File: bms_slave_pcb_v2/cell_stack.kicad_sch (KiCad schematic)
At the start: 33 parts, among them J10 Module Bottom Left FPC Female, J11 Module Bottom Right FPC Female, J4 Module Top Left FPC Female, J5 Module Top Right FPC Female, J6 Breadboard pins for testing, J7 Breadboard pins for testing, J8 Breadboard pins for testing, J9 Breadboard pins for testing

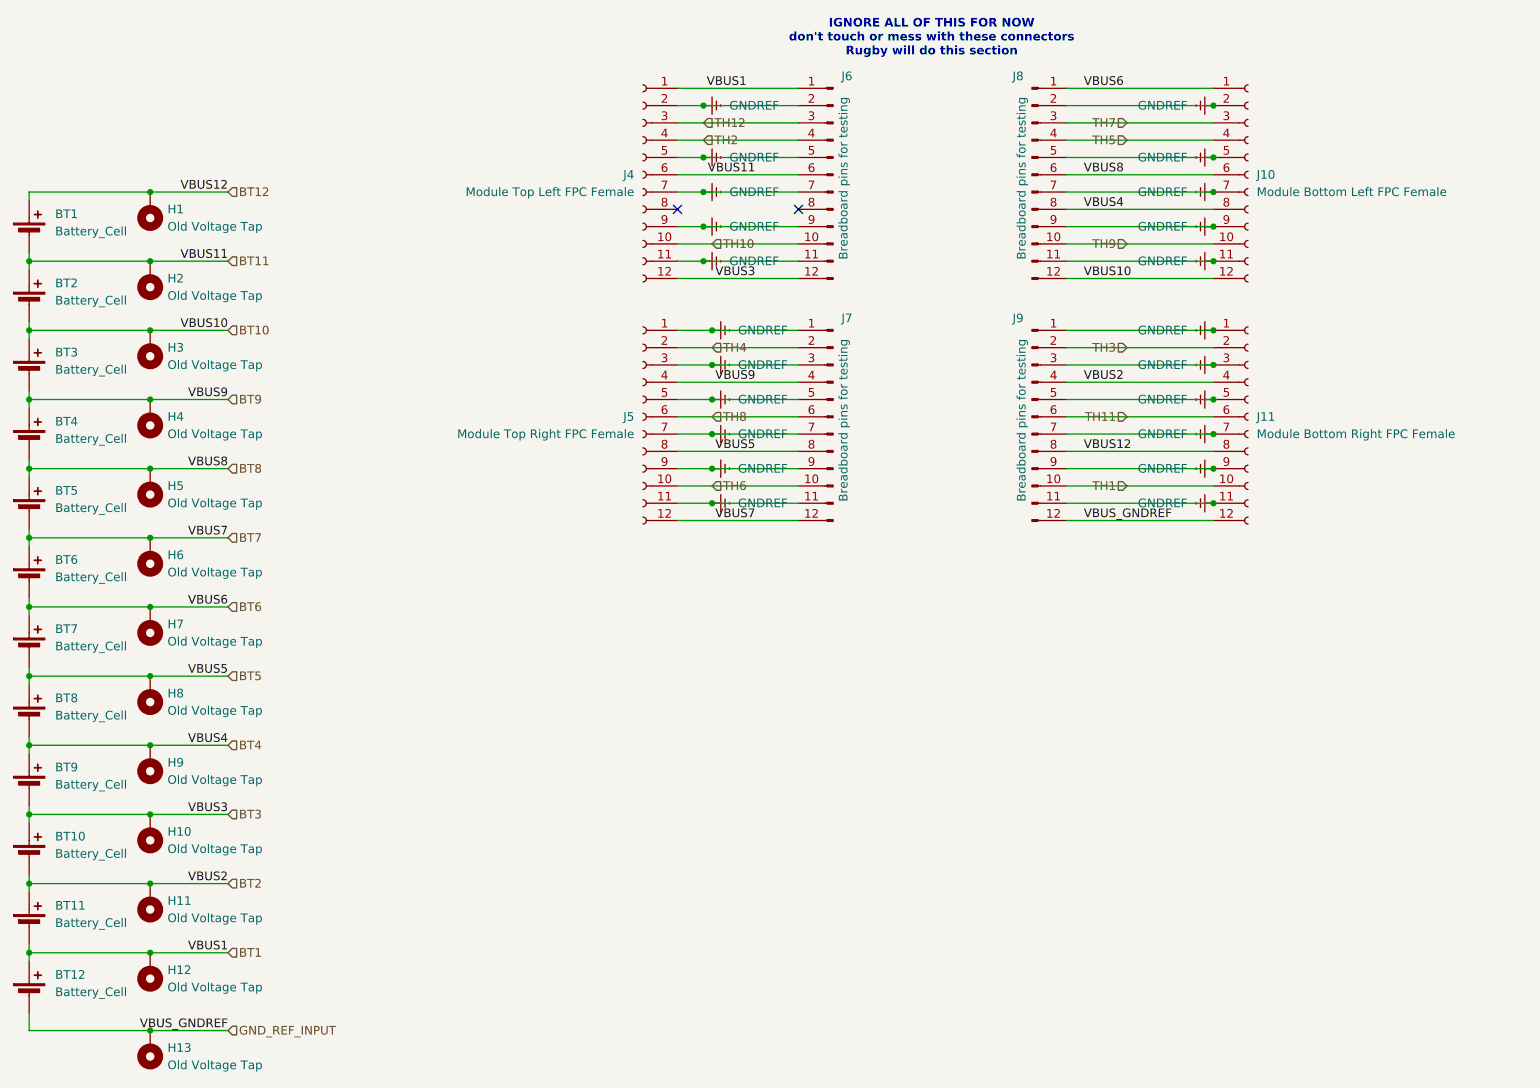
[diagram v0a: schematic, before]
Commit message: Fixed filenames in BMS Slave PCB V2.01, added equipment wishlist
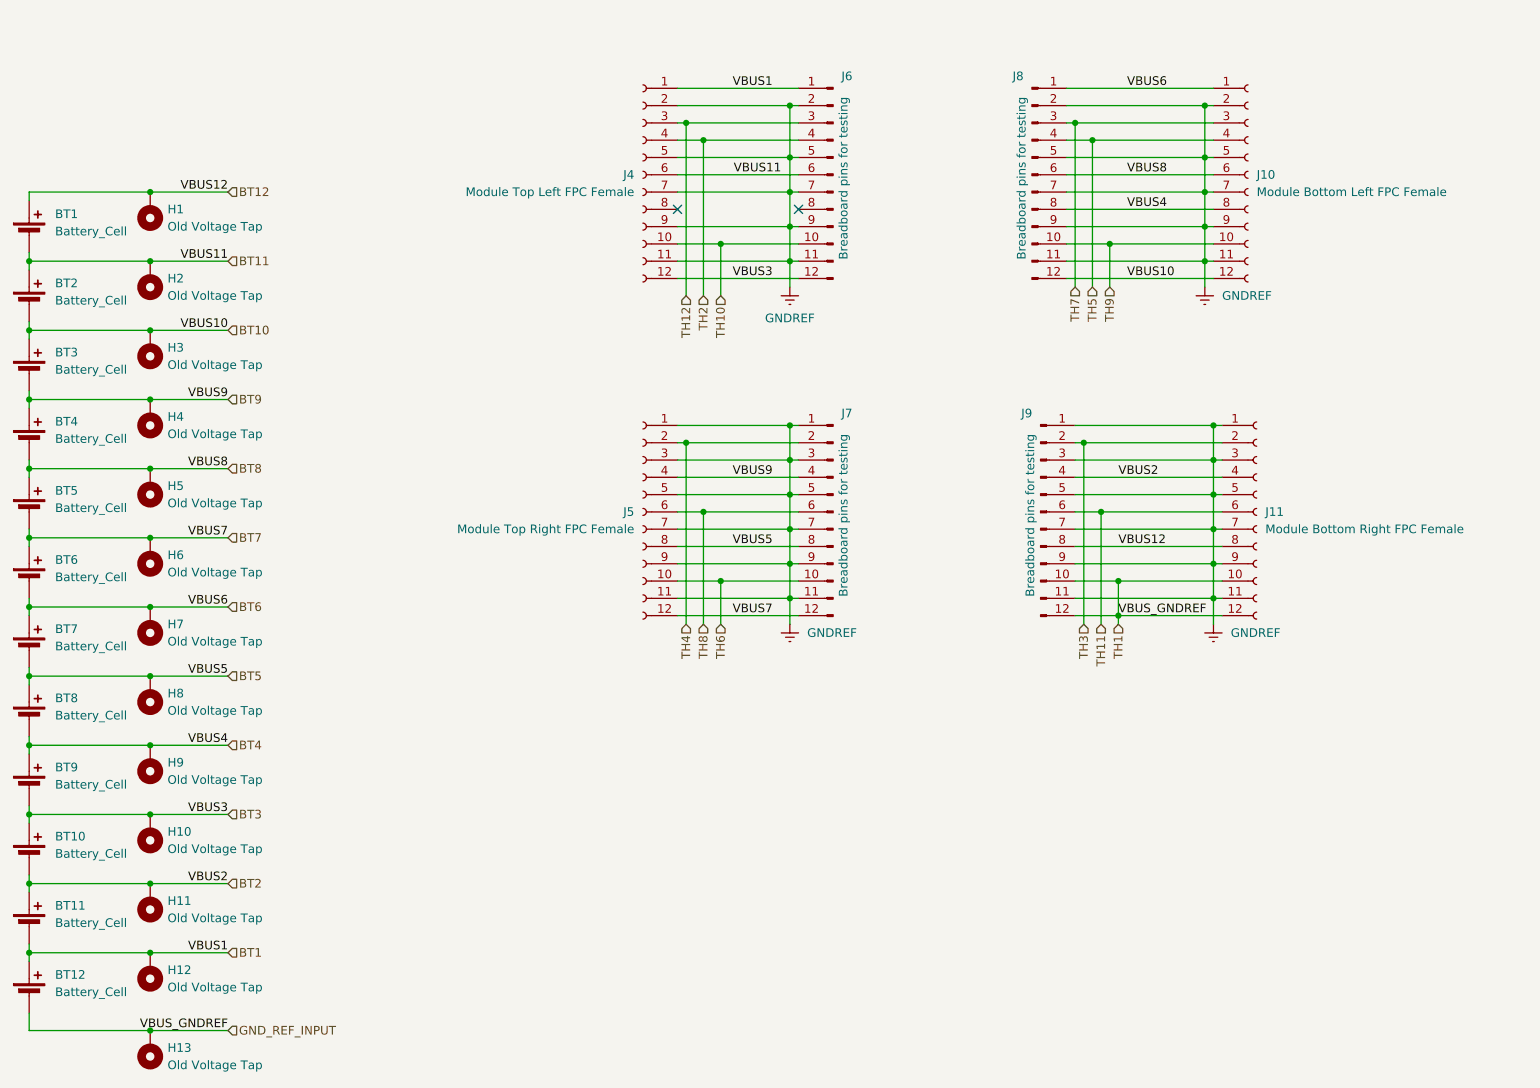
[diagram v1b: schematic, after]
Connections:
- net TH1 is gone; now on net GND_REF_INPUT: J11.10 (Pin_10), J9.10 (Pin_10)
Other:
- note removed: "IGNORE ALL OF THIS FOR NOW don't touch or mess with these connectors Rugby will do this section"
- moved on the sheet: J11, J5, J7, J9
